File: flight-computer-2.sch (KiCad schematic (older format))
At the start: 76 parts, among them J1 USB4105-GF-A, J2 THR, J3 SER1, J4 SER2, J5 SER3, J6 SER4, J7 Breakout, SW1 RESET, SW2 BOOT, U1 AP2114H-3.3TRG1, U2 MUN5214DW1T1G, U3 BNO080, U4 CP2102N, U5 MPL3115A2, U6 ESP32-PICO-D4, Y1 32.768kHz

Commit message: Added MPNs for passives and modified SW symbols
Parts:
- AE1: MPN (none) -> 0479480001
- C1, C3: MPN (none) -> CL10A475KP8NNNC
- C10, C13, C14, C16, C17, C19, C20, C5, C6, C7: MPN (none) -> CL10B104KB8NNNC
- C11, C15, C4: MPN (none) -> GRM188R61A106KE69D
- C12: MPN (none) -> CL10A105KA8NNNC
- C8, C9: MPN (none) -> C0603C220K4GACTU
- D4: value LTST-C191KGKT -> Green; MPN (none) -> LTST-C191KGKT
- L1: MPN (none) -> RC0402JR-070RL
- R1, R2: MPN (none) -> RC0603FR-075K1L
- R10, R22, R23, R9: MPN (none) -> RC0603FR-071KL
- R11, R19, R20, R21, R4: MPN (none) -> RCS06032K00FKEA
- R12, R24, R5, R6, R7, R8: MPN (none) -> RC0603FR-0710KL
- R13, R14: MPN (none) -> RC0603FR-074K7L
- R15: MPN (none) -> RC0603FR-0722K1L
- R16, R17: MPN (none) -> RC0603FR-072K2L
- R18: MPN (none) -> RC0603FR-0747K5L
- R25: MPN (none) -> RC0603FR-0727KL
- R26: MPN (none) -> RC0603FR-0747KL
- R3: MPN (none) -> RC0603FR-071ML
- SW1, SW2: footprint flight-computer-2:SW_PTS810_SJM_250_SMTR_LFS -> Button_Switch_SMD:SW_SPST_PTS810; symbol flight-computer-2:PTS810_SJM_250_SMTR_LFS -> flight-computer-2:PTS810; MPN PTS810-SJM-250-SMTR-LFS -> PTS810 SJS 250 SMTR LFS
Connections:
- wire segments 213 -> 205

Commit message: Readded 3D model for buttons
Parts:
- SW1, SW2: footprint Button_Switch_SMD:SW_SPST_PTS810 -> flight-computer-2:SW_SPST_PTS810
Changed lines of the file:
@@
 Sheet 1 1
 Title "VTOL EDF Flight Computer"
-Date "2020-07-29"
+Date "2020-08-04"
 Rev "v2"
 Comp ""
@@
 F 0 "SW1" H 8350 6031 50  0000 C CNN
 F 1 "RESET" H 8350 5940 50  0000 C CNN
-F 2 "Button_Switch_SMD:SW_SPST_PTS810" H 7800 5600 50  0001 L BNN
+F 2 "flight-computer-2:SW_SPST_PTS810" H 7800 5600 50  0001 L BNN
 F 3 "~" H 8350 5850 50  0001 L BNN
 F 4 "PTS810 SJS 250 SMTR LFS" H 8350 5850 50  0001 C CNN "MPN"
@@
 F 0 "SW2" H 10050 6031 50  0000 C CNN
 F 1 "BOOT" H 10050 5940 50  0000 C CNN
-F 2 "Button_Switch_SMD:SW_SPST_PTS810" H 9500 5600 50  0001 L BNN
+F 2 "flight-computer-2:SW_SPST_PTS810" H 9500 5600 50  0001 L BNN
 F 3 "~" H 10050 5850 50  0001 L BNN
 F 4 "PTS810 SJS 250 SMTR LFS" H 10050 5850 50  0001 C CNN "MPN"

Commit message: More silkscreen fixes and switched MPN
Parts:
- D1, D2: MPN PDS4150-13 -> SM5817PL-TP
- R11, R19, R20, R21, R4: MPN RCS06032K00FKEA -> RC0603FR-072KL
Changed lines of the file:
@@
 F 2 "flight-computer-2:D_SOD-123F" H 3000 5050 50  0001 C CNN
 F 3 "~" H 3000 5050 50  0001 C CNN
-F 4 "PDS4150-13" H 3000 5050 50  0001 C CNN "MPN"
+F 4 "SM5817PL-TP" H 3000 5050 50  0001 C CNN "MPN"
 	1    3000 5050
 	-1   0    0    1
@@
 F 2 "Resistor_SMD:R_0603_1608Metric" H 3200 1300 50  0001 C CNN
 F 3 "~" H 3200 1300 50  0001 C CNN
-F 4 "RCS06032K00FKEA" H 3200 1300 50  0001 C CNN "MPN"
+F 4 "RC0603FR-072KL" H 3200 1300 50  0001 C CNN "MPN"
 	1    3200 1300
 	1    0    0    -1
@@
 F 2 "Resistor_SMD:R_0603_1608Metric" H 4250 6600 50  0001 C CNN
 F 3 "~" H 4250 6600 50  0001 C CNN
-F 4 "RCS06032K00FKEA" H 4250 6600 50  0001 C CNN "MPN"
+F 4 "RC0603FR-072KL" H 4250 6600 50  0001 C CNN "MPN"
 	1    4250 6600
 	0    1    1    0
@@
 F 2 "flight-computer-2:D_SOD-123F" H 1400 2500 50  0001 C CNN
 F 3 "~" H 1400 2500 50  0001 C CNN
-F 4 "PDS4150-13" H 1400 2500 50  0001 C CNN "MPN"
+F 4 "SM5817PL-TP" H 1400 2500 50  0001 C CNN "MPN"
 	1    1400 2500
 	1    0    0    -1
@@
 F 2 "Resistor_SMD:R_0603_1608Metric" H 9600 4750 50  0001 C CNN
 F 3 "~" H 9600 4750 50  0001 C CNN
-F 4 "RCS06032K00FKEA" H 9600 4750 50  0001 C CNN "MPN"
+F 4 "RC0603FR-072KL" H 9600 4750 50  0001 C CNN "MPN"
 	1    9600 4750
 	0    -1   -1   0
@@
 F 2 "Resistor_SMD:R_0603_1608Metric" H 7350 3050 50  0001 C CNN
 F 3 "~" H 7350 3050 50  0001 C CNN
-F 4 "RCS06032K00FKEA" H 7350 3050 50  0001 C CNN "MPN"
+F 4 "RC0603FR-072KL" H 7350 3050 50  0001 C CNN "MPN"
 	1    7350 3050
 	-1   0    0    1
@@
 F 2 "Resistor_SMD:R_0603_1608Metric" H 7050 3050 50  0001 C CNN
 F 3 "~" H 7050 3050 50  0001 C CNN
-F 4 "RCS06032K00FKEA" H 7050 3050 50  0001 C CNN "MPN"
+F 4 "RC0603FR-072KL" H 7050 3050 50  0001 C CNN "MPN"
 	1    7050 3050
 	1    0    0    1

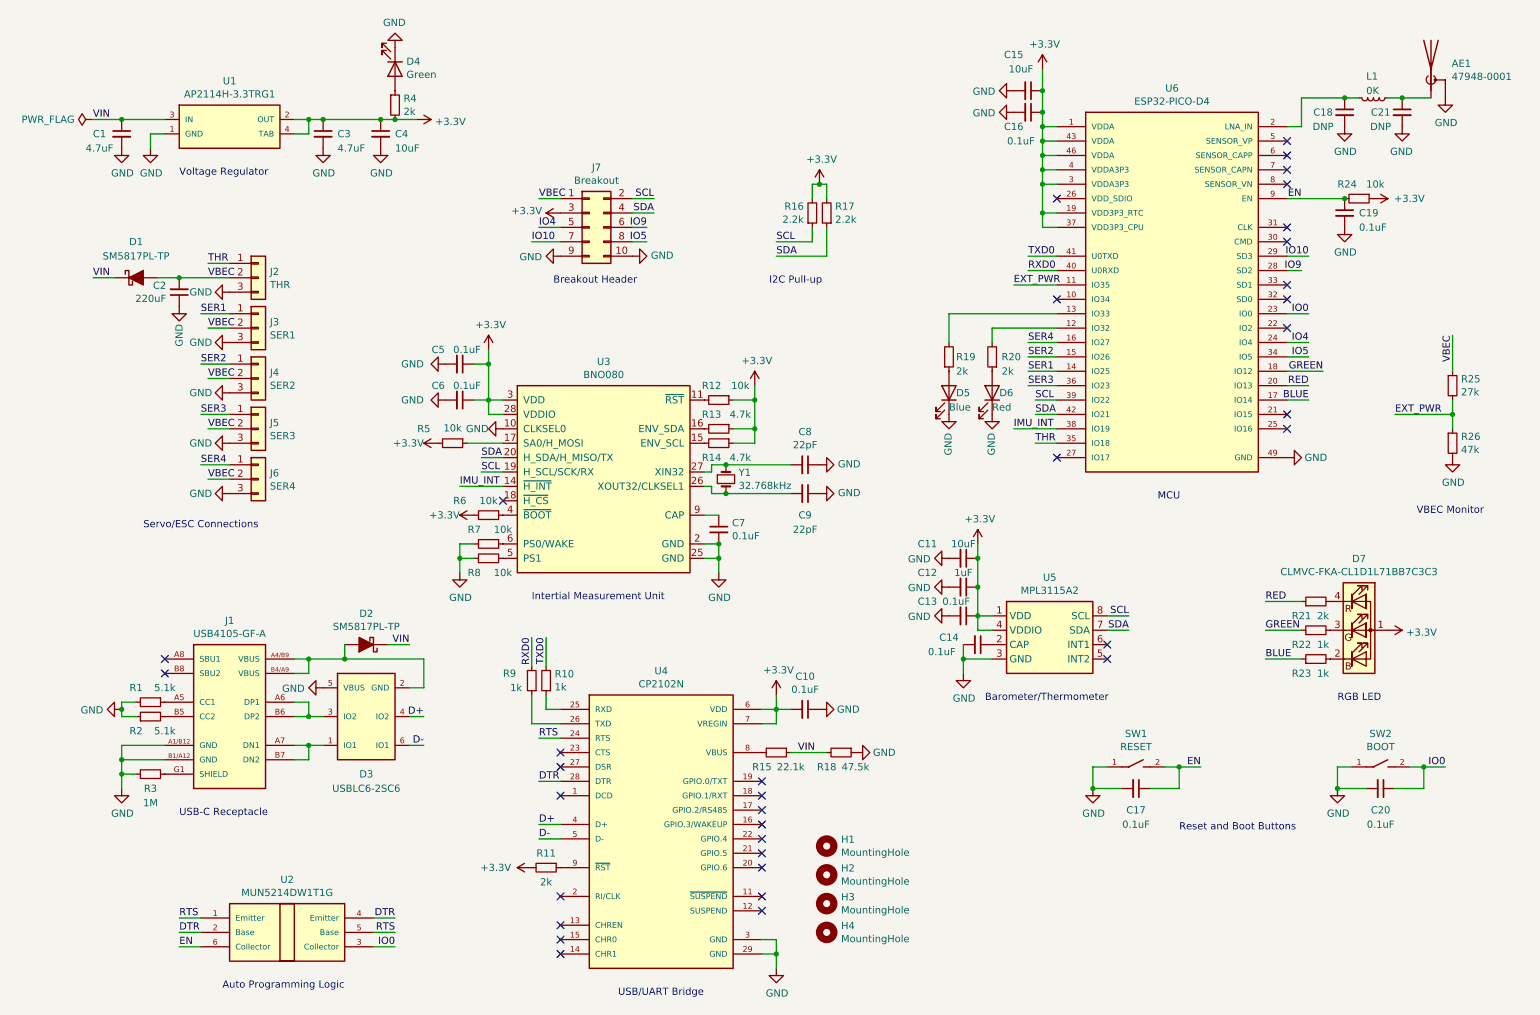
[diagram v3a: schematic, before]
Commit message: Switching to ESP32-MINI-1 module
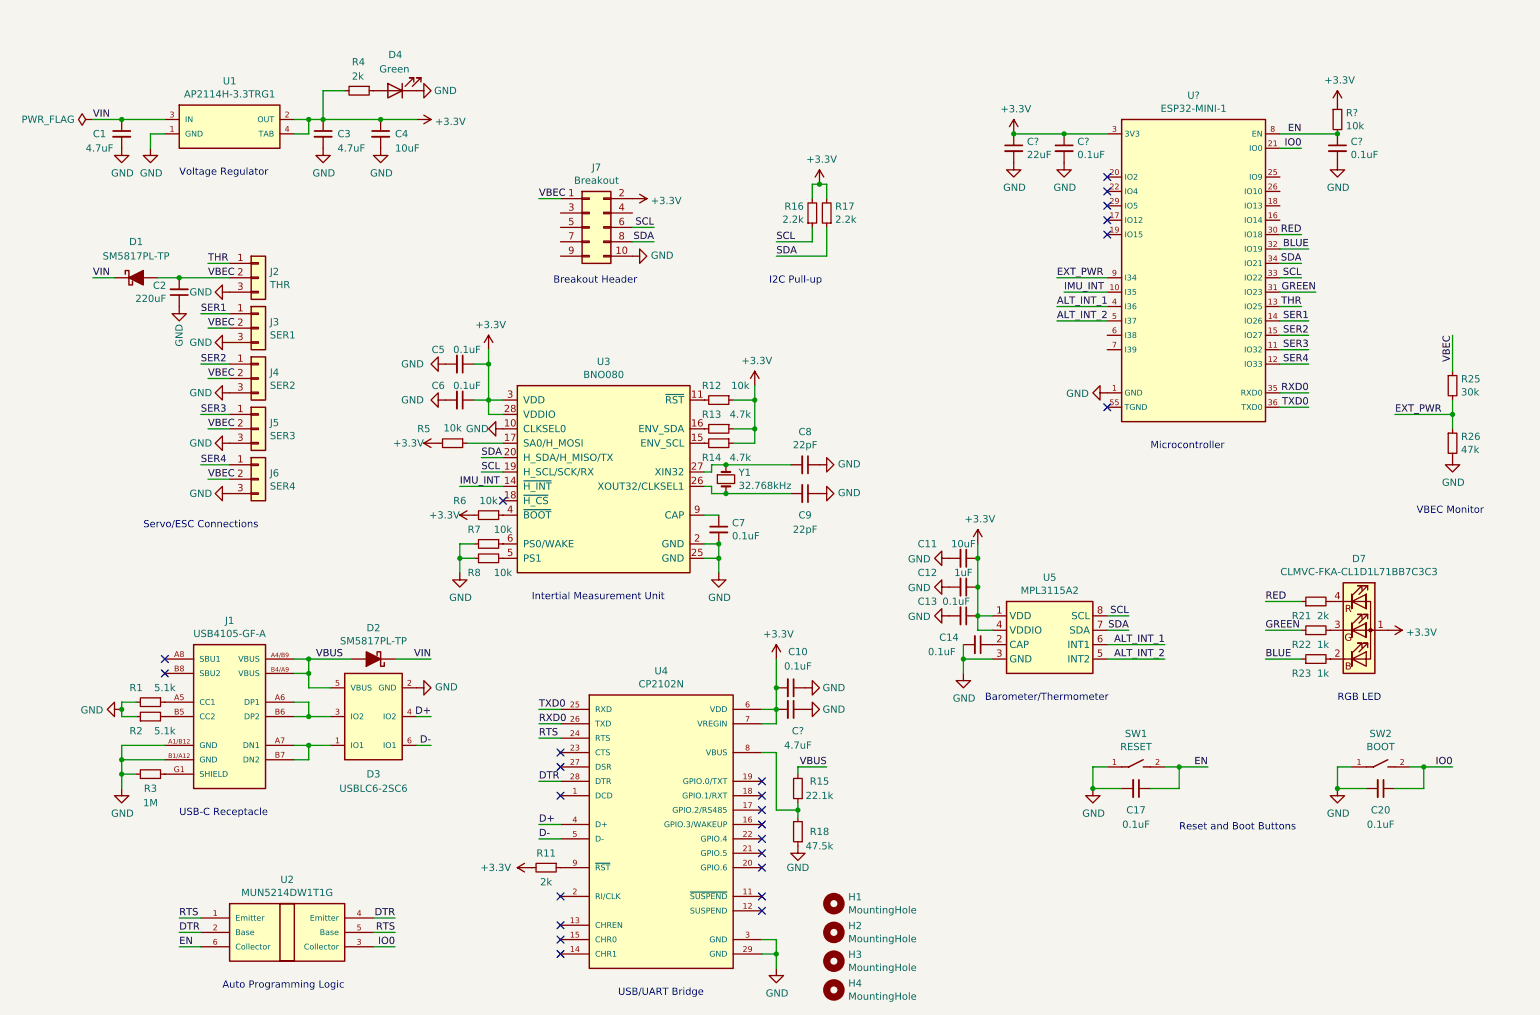
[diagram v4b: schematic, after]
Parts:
- removed AE1: 47948-0001, flight-computer-2:47948-0001, symbol flight-computer-2:47948-0001
- removed C15: 10uF, Capacitor_SMD:C_0603_1608Metric, symbol Device:C_Small
- removed C16, C19: 0.1uF, Capacitor_SMD:C_0603_1608Metric, symbol Device:C_Small
- removed C18, C21: DNP, Capacitor_SMD:C_0402_1005Metric, symbol Device:C_Small
- removed D5: Blue, LED_SMD:LED_0603_1608Metric, symbol Device:LED
- removed D6: Red, LED_SMD:LED_0603_1608Metric, symbol Device:LED
- removed L1: 0K, Inductor_SMD:L_0402_1005Metric, symbol Device:L_Small
- removed R10, R9: 1k, Resistor_SMD:R_0603_1608Metric, symbol Device:R_Small
- removed R19, R20: 2k, Resistor_SMD:R_0603_1608Metric, symbol Device:R_Small
- removed R24: 10k, Resistor_SMD:R_0603_1608Metric, symbol Device:R_Small
- removed U6: ESP32-PICO-D4, flight-computer-2:ESP32_PICO_D4, symbol flight-computer-2:ESP32-PICO-D4
- added C?: 4.7uF, Capacitor_SMD:C_0603_1608Metric, symbol Device:C_Small
- added C?: 22uF, symbol Device:C_Small
- added C? (x2): 0.1uF, symbol Device:C_Small
- added R?: 10k, symbol Device:R_Small
- added U?: ESP32-MINI-1, symbol flight-computer-2:ESP32-MINI-1
- R25: value 27k -> 30k
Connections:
- net IO5 is gone; now on net SDA: J7.8 (Pin_8)
- net IO9 is gone; now on net SCL: J7.6 (Pin_6)
- net +3V3: now also J7.2 (Pin_2), C?.1, C?.1, C?.2, R?.1, U?.3 (3V3); no longer J7.3 (Pin_3)
- net BLUE: now also U?.32 (IO19)
- net EN: now also C?.1, R?.2, U?.8 (EN)
- net EXT_PWR: now also U?.9 (I34)
- net GND: now also D3.2 (GND), C?.1, C?.2, C?.2, C?.2, U?.1 (GND), U?.2 (GND), U?.27 (GND), U?.38 (GND), U?.39 (GND), U?.40 (GND), U?.41 (GND), U?.42 (GND), U?.43 (GND), U?.44 (GND), U?.45 (GND), U?.46 (GND), U?.47 (GND), U?.48 (GND), U?.49 (GND), U?.50 (GND), U?.51 (GND), U?.52 (GND), U?.53 (GND), U?.54 (GND); no longer D3.5 (VBUS), J7.9 (Pin_9)
- net GREEN: now also U?.31 (IO23)
- net IMU_INT: now also U?.10 (I35)
- net IO0: now also U?.21 (IO0)
- net RED: now also U?.30 (IO18)
- net RXD0: now also U4.26 (TXD), U?.35 (RXD0)
- net SCL: now also U?.33 (IO22); no longer J7.2 (Pin_2)
- net SDA: now also U?.34 (IO21); no longer J7.4 (Pin_4)
- net SER1: now also U?.14 (IO26)
- net SER2: now also U?.15 (IO27)
- net SER3: now also U?.11 (IO32)
- net SER4: now also U?.12 (IO33)
- net THR: now also U?.13 (IO25)
- net TXD0: now also U4.25 (RXD), U?.36 (TXD0)
- net VIN: no longer R15.1, R18.2
- net VBUS: now reaches D2.2 (A), J1.A4/B9 (VBUS), J1.B4/A9 (VBUS)
- net VBUS: now also D3.5 (VBUS), R15.2; no longer D3.2 (GND)
- net at U4.8 (VBUS): now also R15.1, R18.2; no longer R15.2
- net ALT_INT_2: now reaches U5.5 (INT2)
- net ALT_INT_2: now also U?.5 (I37)
- net ALT_INT_1: now reaches U5.6 (INT1)
- net ALT_INT_1: now also U?.4 (I36)
- net IO10: no longer names the net of J7.7 (Pin_7)
- net IO4: no longer names the net of J7.5 (Pin_5)
- no-connect marks 35 -> 25
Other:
- note added: "Microcontroller"
- note removed: "MCU"
- moved on the sheet: C10, D2, D3, D4, H1, H2, H3, H4, R15, R18, R4

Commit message: Status LED and breakout pins
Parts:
- added D?: Blue, LED_SMD:LED_0603_1608Metric, symbol Device:LED
- added R?: 2k, Resistor_SMD:R_0603_1608Metric, symbol Device:R_Small
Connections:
- net GND: now also D?.1 (K)
- net EXT1: now reaches J7.3 (Pin_3)
- net EXT1: now also U?.25 (IO9)
- net IO5: now reaches J7.4 (Pin_4)
- net IO5: now also U?.29 (IO5)
- net EXT2: now reaches J7.5 (Pin_5)
- net EXT2: now also U?.26 (IO10)
- net EXT3: now reaches J7.7 (Pin_7)
- net EXT3: now also U?.18 (IO13)
- net EXT4: now reaches J7.9 (Pin_9)
- net EXT4: now also U?.16 (IO14)
- net at U?.19 (IO15): now also R?.2
- new net: D?.2 (A), R?.1
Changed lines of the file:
@@
 NoConn ~ 8150 1800
 NoConn ~ 8150 1900
-NoConn ~ 8150 2000
 NoConn ~ 8150 2100
-NoConn ~ 8150 2200
 $Comp
 L power:GND #PWR0102
@@
 Text Notes 8450 3700 0    50   ~ 0
 Microcontroller
+Text Label 9550 1800 2    50   ~ 0
+EXT1
+Text Label 9550 1900 2    50   ~ 0
+EXT2
+Text Label 9550 2000 2    50   ~ 0
+EXT3
+Text Label 9550 2100 2    50   ~ 0
+EXT4
+Wire Wire Line
+	9350 1800 9550 1800
+Wire Wire Line
+	9350 1900 9550 1900
+Wire Wire Line
+	9350 2000 9550 2000
+Wire Wire Line
+	9350 2100 9550 2100
+Text Label 4200 2050 0    50   ~ 0
+EXT1
+Text Label 4200 2150 0    50   ~ 0
+EXT2
+Text Label 4200 2250 0    50   ~ 0
+EXT3
+Text Label 4200 2350 0    50   ~ 0
+EXT4
+Wire Wire Line
+	4350 2050 4200 2050
+Wire Wire Line
+	4350 2150 4200 2150
+Wire Wire Line
+	4350 2250 4200 2250
+Wire Wire Line
+	4350 2350 4200 2350
+NoConn ~ 8150 2900
+NoConn ~ 8150 3000
+$Comp
+L Device:LED D?
+U 1 1 607AD60F
+P 7800 2200
+F 0 "D?" H 7750 2300 50  0000 L CNN
+F 1 "Blue" H 7750 2100 50  0000 L CNN
+F 2 "LED_SMD:LED_0603_1608Metric" H 7800 2200 50  0001 C CNN
+F 3 "~" H 7800 2200 50  0001 C CNN
+F 4 "LTST-C191TBKT" H 7800 2200 50  0001 C CNN "MPN"
+	1    7800 2200
+	1    0    0    1
+$EndComp
+$Comp
+L power:GND #PWR?
+U 1 1 607AD615
+P 7650 2200
+F 0 "#PWR?" H 7650 1950 50  0001 C CNN
+F 1 "GND" V 7650 2000 50  0000 C CNN
+F 2 "" H 7650 2200 50  0001 C CNN
+F 3 "" H 7650 2200 50  0001 C CNN
+	1    7650 2200
+	0    1    -1   0
+$EndComp
+$Comp
+L Device:R_Small R?
+U 1 1 607AD61C
+P 8050 2200
+F 0 "R?" V 8150 2200 50  0000 L CNN
+F 1 "2k" V 8150 2050 50  0000 L CNN
+F 2 "Resistor_SMD:R_0603_1608Metric" H 8050 2200 50  0001 C CNN
+F 3 "~" H 8050 2200 50  0001 C CNN
+F 4 "RC0603FR-072KL" H 8050 2200 50  0001 C CNN "MPN"
+	1    8050 2200
+	0    -1   1    0
+$EndComp
+Text Label 8000 2000 0    50   ~ 0
+IO5
+Wire Wire Line
+	8000 2000 8150 2000
+Text Label 4950 2050 2    50   ~ 0
+IO5
+Wire Wire Line
+	4950 2050 4850 2050
 $EndSCHEMATC

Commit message: BNO upgrade and address selection
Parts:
- U3: value BNO080 -> BNO085; symbol flight-computer-2:BNO080 -> flight-computer-2:BNO085; MPN BNO080 -> BNO085
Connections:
- net +3V3: no longer R5.2
- net GND: now also R5.2
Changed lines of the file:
@@
 	0    1    1    0
-$EndComp
-$Comp
-L power:+3.3V #PWR016
-U 1 1 5F525B03
-P 3500 3650
-F 0 "#PWR016" H 3500 3500 50  0001 C CNN
-F 1 "+3.3V" V 3500 3750 50  0000 L CNN
-F 2 "" H 3500 3650 50  0001 C CNN
-F 3 "" H 3500 3650 50  0001 C CNN
-	1    3500 3650
-	0    -1   -1   0
 $EndComp
 Wire Wire Line
@@
 	9500 5150 9250 5150
 $Comp
-L flight-computer-2:BNO080 U3
+L flight-computer-2:BNO085 U3
 U 1 1 5F4112EB
 P 4650 3100
 F 0 "U3" H 4650 3117 50  0000 C CNN
-F 1 "BNO080" H 4650 3026 50  0000 C CNN
+F 1 "BNO085" H 4650 3026 50  0000 C CNN
 F 2 "flight-computer-2:LGA-28_5.2x3.8mm_P0.5mm" H 4650 3100 50  0001 C CNN
 F 3 "" H 4650 3100 50  0001 C CNN
-F 4 "BNO080" H 4650 3100 50  0001 C CNN "MPN"
+F 4 "BNO085" H 4650 3100 50  0001 C CNN "MPN"
 	1    4650 3100
 	1    0    0    -1
@@
 Wire Wire Line
 	4950 2050 4850 2050
+$Comp
+L power:GND #PWR?
+U 1 1 607DAC02
+P 3500 3650
+F 0 "#PWR?" H 3500 3400 50  0001 C CNN
+F 1 "GND" V 3505 3522 50  0000 R CNN
+F 2 "" H 3500 3650 50  0001 C CNN
+F 3 "" H 3500 3650 50  0001 C CNN
+	1    3500 3650
+	0    1    1    0
+$EndComp
 $EndSCHEMATC
